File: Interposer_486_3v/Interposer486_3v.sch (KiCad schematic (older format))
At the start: 243 parts, among them J1 WB/~WT, J2 CLKMUL, J3 V Select, U1 LT1085-ADJ

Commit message: Rename Interposer_486_3v folder.
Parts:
- added CN1: +5v External, Connector_Wire:SolderWirePad_1x01_SMD_1x2mm, symbol Connector_Generic:Conn_01x01
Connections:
- net +5V: now also CN1.1 (Pin_1)
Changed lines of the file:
@@
 	-1   0    0    1
 $EndComp
+$Comp
+L power:+5V #PWR0104
+U 1 1 6104E286
+P 14350 1600
+F 0 "#PWR0104" H 14350 1450 50  0001 C CNN
+F 1 "+5V" H 14365 1773 50  0000 C CNN
+F 2 "" H 14350 1600 50  0001 C CNN
+F 3 "" H 14350 1600 50  0001 C CNN
+	1    14350 1600
+	1    0    0    -1
+$EndComp
+Wire Wire Line
+	14450 1700 14350 1700
+Wire Wire Line
+	14350 1700 14350 1600
+$Comp
+L Connector_Generic:Conn_01x01 CN1
+U 1 1 6104B845
+P 14650 1700
+F 0 "CN1" H 14730 1742 50  0000 L CNN
+F 1 "+5v External" H 14730 1651 50  0000 L CNN
+F 2 "Connector_Wire:SolderWirePad_1x01_SMD_1x2mm" H 14650 1700 50  0001 C CNN
+F 3 "~" H 14650 1700 50  0001 C CNN
+	1    14650 1700
+	1    0    0    -1
+$EndComp
 $EndSCHEMATC

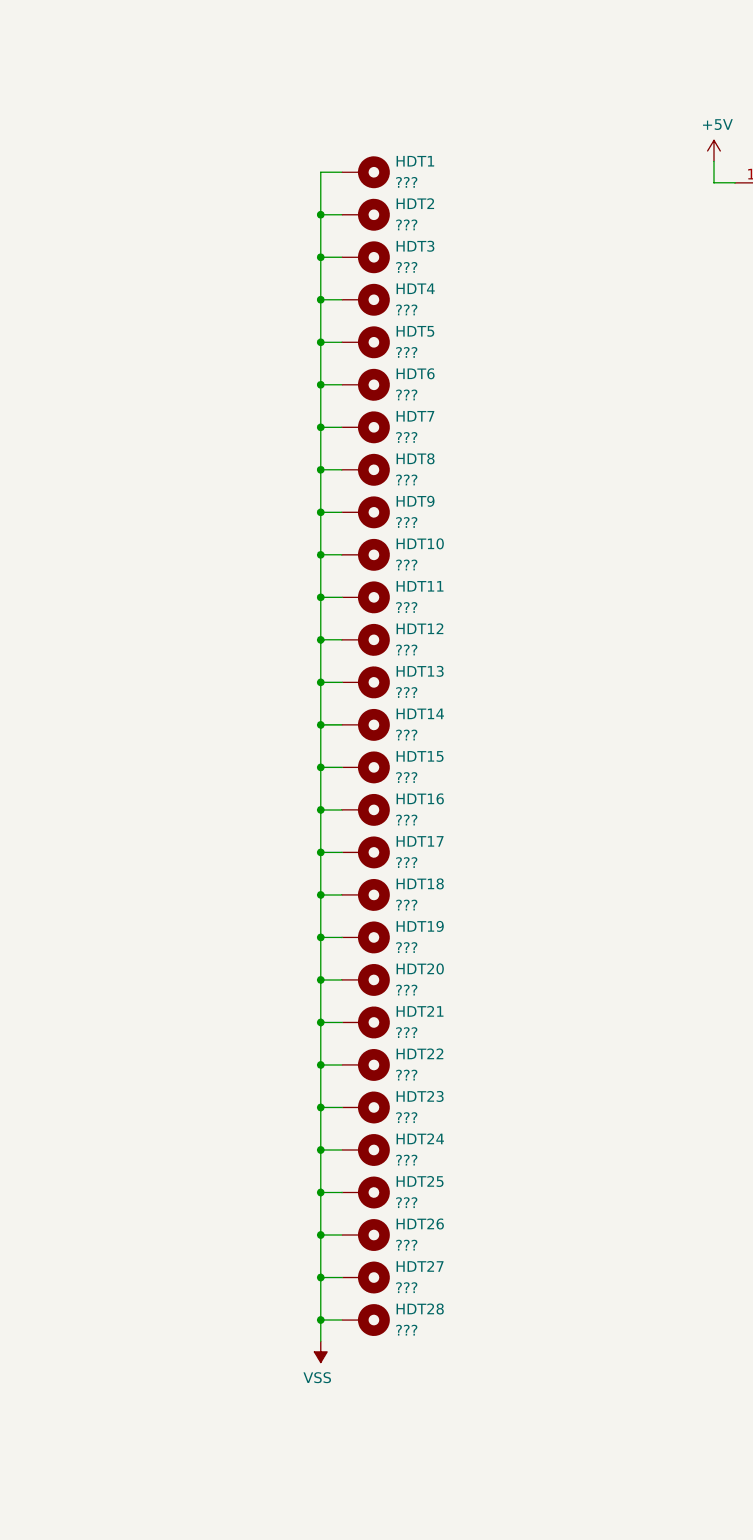
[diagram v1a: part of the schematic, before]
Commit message: Remove drill template from 486 3v interposer.
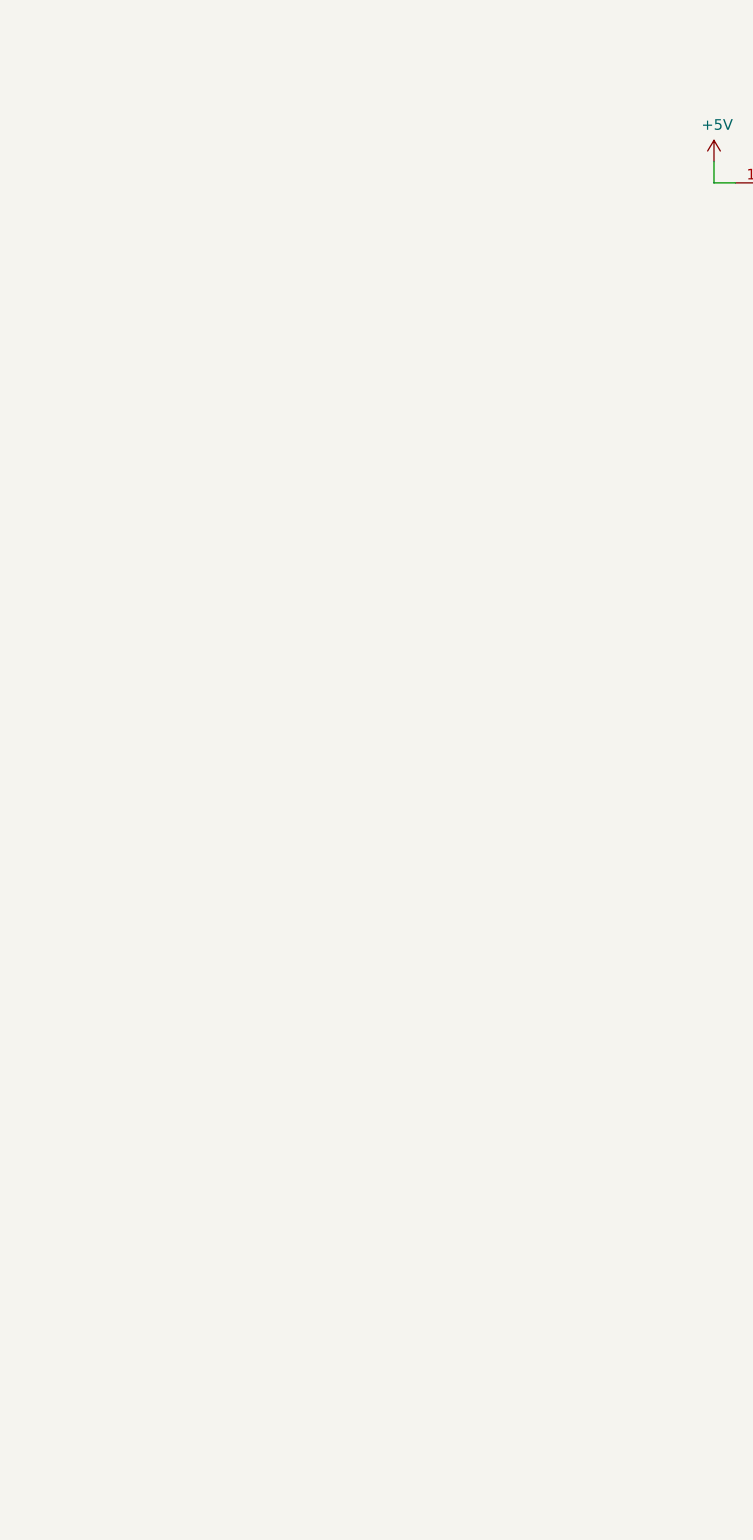
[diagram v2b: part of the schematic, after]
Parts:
- removed HDT1, HDT10, HDT11, HDT12, HDT13, HDT14, HDT15, HDT16, HDT17, HDT18, HDT19, HDT2, HDT20, HDT21, HDT22, HDT23, HDT24, HDT25, HDT26, HDT27, HDT28, HDT3, HDT4, HDT5, HDT6, HDT7, HDT8, HDT9: ???, 00Custom:MachinePinHole, symbol Mechanical:MountingHole_Pad
